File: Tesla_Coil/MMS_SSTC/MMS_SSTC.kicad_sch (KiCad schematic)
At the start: 57 parts, among them J1 Screw_Terminal_01x02, J2 Screw_Terminal_01x02, J3 Screw_Terminal_01x02, J4 Screw_Terminal_01x02, Q1 IRFP460APBF, U1 LM7812_TO220, U2 LM7805_TO220, U3 CD74HC14E, U4 UCC27524P, U5 NE555P

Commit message: Begin work on final tesla coil design
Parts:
- removed AE1: Antenna, TestPoint:TestPoint_Keystone_5000-5004_Miniature, symbol Device:Antenna
- removed C1, C3: 470u, Capacitor_THT:CP_Radial_D12.5mm_P5.00mm, symbol Device:C_Polarized_Small
- removed C13, C17: 10n, Capacitor_THT:C_Disc_D5.0mm_W2.5mm_P2.50mm, symbol Device:C_Small
- removed C15, C16: 1.5n, Capacitor_THT:C_Rect_L13.0mm_W4.0mm_P10.00mm_FKS3_FKP3_MKS4, symbol Device:C_Small
- removed C2, C4, C5: 0.1u, Capacitor_THT:C_Disc_D3.0mm_W2.0mm_P2.50mm, symbol Device:C_Small
- removed C6, C7: 2200u, Capacitor_THT:CP_Radial_D25.0mm_P10.00mm_SnapIn, symbol Device:C_Polarized_Small
- removed C8: 0.68u, Capacitor_THT:C_Rect_L7.2mm_W5.5mm_P5.00mm_FKS2_FKP2_MKS2_MKP2, symbol Device:C_Small
- removed D1: D_Filled, Diode_THT:D_DO-41_SOD81_P7.62mm_Horizontal, symbol Device:D_Filled
- removed D2: B125C2300-1500A, Diode_THT:Diode_Bridge_Vishay_GBU, symbol Diode_Bridge:B125C2300-1500A
- removed D3, D6: ~, Diode_THT:D_DO-41_SOD81_P7.62mm_Horizontal, symbol Device:D_Small_Filled
- removed J1, J3: Screw_Terminal_01x02, locals:691137710003, symbol Connector:Screw_Terminal_01x03
- removed J2: Screw_Terminal_01x02, locals:691137710002, symbol Connector:Screw_Terminal_01x02
- removed JP1, JP3, JP4: Jumper_2_Bridged, TestPoint:TestPoint_Bridge_Pitch2.54mm_Drill0.7mm, symbol Jumper:Jumper_2_Bridged
- removed JP2, JP5: Jumper_2_Open, TestPoint:TestPoint_Bridge_Pitch2.54mm_Drill0.7mm, symbol Jumper:Jumper_2_Open
- removed R2: 220k, Resistor_THT:R_Axial_DIN0204_L3.6mm_D1.6mm_P5.08mm_Horizontal, symbol Device:R_US
- removed R5: 1k, Resistor_THT:R_Axial_DIN0204_L3.6mm_D1.6mm_P5.08mm_Horizontal, symbol Device:R_US
- removed TR1: 48VAC, symbol Transformer:TRANSF4
- removed U1: LM7812_TO220, Package_TO_SOT_THT:TO-220-3_Vertical, symbol Regulator_Linear:LM7812_TO220
- removed U2: LM7805_TO220, Package_TO_SOT_THT:TO-220-3_Vertical, symbol Regulator_Linear:LM7805_TO220
- removed U4: UCC27524P, Package_DIP:DIP-8_W7.62mm, symbol locals:UCC27524P
- added D3: 400V, Diode_THT:D_DO-27_P12.70mm_Horizontal, symbol Device:D_TVS_Small_Filled
- added U6: UCC37322P, UCC37322P:DIP794W45P254L959H508Q8, symbol locals:UCC37322P
- C14: value 1.5n -> 2.7n; DKPN 495-3205-ND -> 495-3223-ND
- Q1: value IRFP460APBF -> FQA8N100C; DKPN IRFP460APBF-ND -> FQA8N100CFS-ND
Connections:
- net +12V: now also U6.1 (VDD__1), U6.8 (VDD)
- net Earth: no longer C10.1, C11.1, C12.2, C14.2, C18.2, C19.2, C9.2, D4.1 (A1), D5.1 (A1), Q1.3 (S), U3.7 (GND), U5.1 (GND), U5.7 (DIS)
- net INTERRUPT_OUT: now also U6.3 (ENBL)
- net OSC_OUT: now also U6.2 (IN)
- net at R1.2: now also U6.6 (OUT), U6.7 (OUT__1)
- net at C14.1, J4.3 (Pin_3), Q1.2 (D): now also D3.2 (A2); no longer D4.2 (A2)
- net +68V renamed +170V
- new net: D3.1 (A1), D4.2 (A2)
- new net GND: C10.1, C11.1, C12.2, C14.2, C18.2, C19.2, C9.2, D4.1 (A1), D5.1 (A1), Q1.3 (S), U3.7 (GND), U5.1 (GND), U5.7 (DIS), U6.4 (AGND), U6.5 (PGND)
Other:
- note added: "2x 1.5n 5% also viable but less tolerance stackup will make things easier"
- note added: "EARTH GROUND ONLY!"
- note added: "Note: C19 should be stable and well toleranced if using fixed values"
- note added: "renumber this bs for the schematic later"
- note added: "terminal blocks for primary coil need to be impossible to touch when put together"
- note removed: "150k also viable"
- note removed: "Antenna feedback: Connect JP3, disconnect JP4 Oscillator: Disonnect JP3, connect JP4 C/W output: Disconnect JP2, connect JP1 Antenna cap test: Disconnect JP5"
- note removed: "D3 and D6 *must* have forward voltage <0.5 and be schottky"
- note removed: "Note: C19 should be stable and high quality if using fixed values"
- note removed: "Primary between 2-3 Secondary ground on 1"
- note removed: "R5 for current limiting short if problems"
- note removed: "Try desoldering one of the big caps just to see what happens"
- note removed: "power delivery deserves its own separate page </3"
- moved on the sheet: C10, C11, C12, C14, C18, C19, C9, D4, D5, D7, D8, J4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

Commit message: Draft BOM for final SSTC design
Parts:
- removed D8: D_Small_Filled, Diode_THT:D_DO-41_SOD81_P7.62mm_Horizontal, symbol Device:D_Small_Filled
- removed R3: 1k, Resistor_THT:R_Axial_DIN0204_L3.6mm_D1.6mm_P5.08mm_Horizontal, symbol Device:R_US
- removed RV2, RV3: R_Potentiometer_Trim_US, Potentiometer_THT:Potentiometer_Bourns_3296W_Vertical, symbol Device:R_Potentiometer_Trim_US
- added R1: 18k, Resistor_THT:R_Axial_DIN0204_L3.6mm_D1.6mm_P5.08mm_Horizontal, symbol Device:R_Small_US
- added R2: 150k, Resistor_THT:R_Axial_DIN0204_L3.6mm_D1.6mm_P5.08mm_Horizontal, symbol Device:R_Small_US
- D1: renamed from D7; footprint Diode_THT:D_DO-41_SOD81_P7.62mm_Horizontal -> Diode_THT:D_DO-35_SOD27_P7.62mm_Horizontal; DKPN 1N4004-TPMSCT-ND -> 497-2499-1-ND
- RV1: footprint Potentiometer_THT:Potentiometer_Bourns_3296W_Vertical -> Potentiometer_THT:Potentiometer_Bourns_3296X_Horizontal; DKPN 118-3296W-1-103RLFCT-ND -> 118-3296X-1-222LF-ND
- U1: renamed from U5; footprint Package_DIP:DIP-8_W7.62mm -> Package_DIP:DIP-8_W7.62mm_Socket
- U2: renamed from U6; footprint UCC37322P:DIP794W45P254L959H508Q8 -> Package_DIP:DIP-8_W7.62mm_Socket
- renumbered AE2 to AE1, C18 to C1, C12 to C2, C19 to C3, C9 to C4, C11 to C5, C14 to C6, C10 to C7, D5 to D2, J4 to J1, R1 to R3
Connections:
- net GND: no longer U1.7 (DIS)
- net INTERRUPT_OUT: now also D1.2 (A)
- net at C3.1, U1.2 (TR), U1.6 (THR): now also R1.2, R2.2
- net at D1.1 (K): now also R1.1
- new net: R2.1, U1.7 (DIS)
- no-connect marks 11 -> 9
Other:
- moved on the sheet: C2, C3, D1

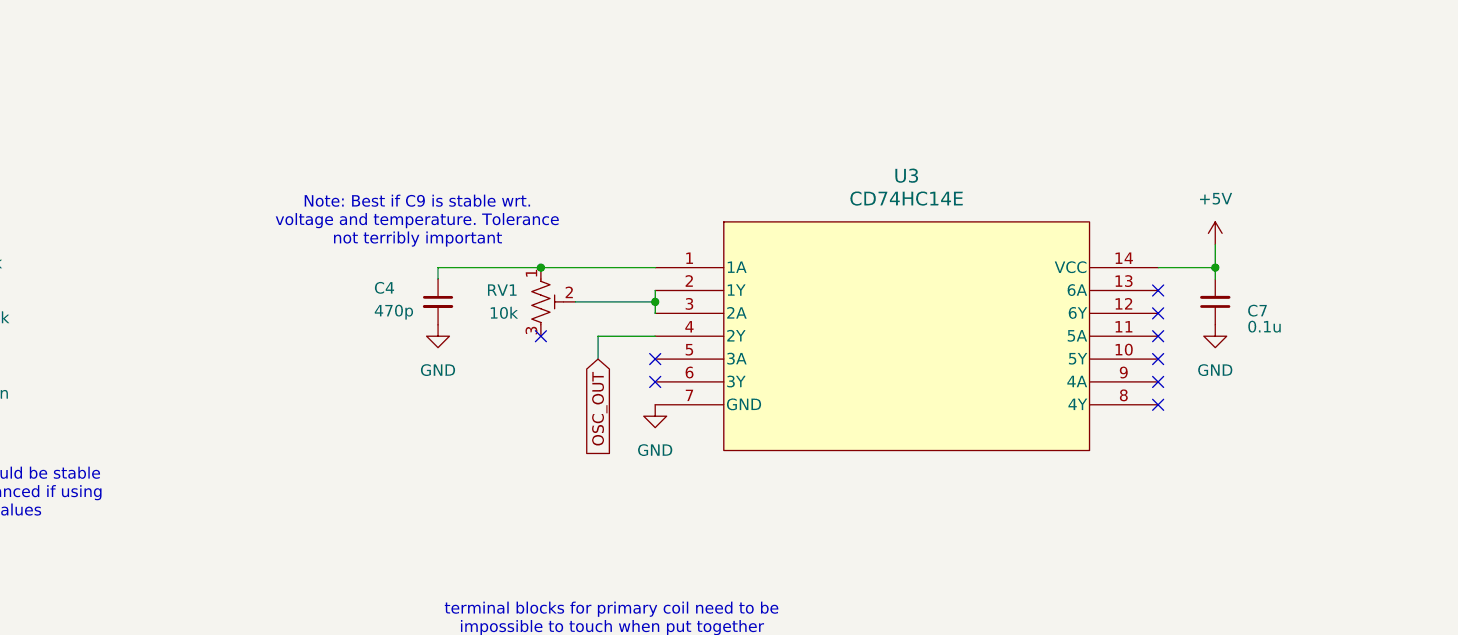
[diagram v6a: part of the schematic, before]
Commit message: apply cost saving measures
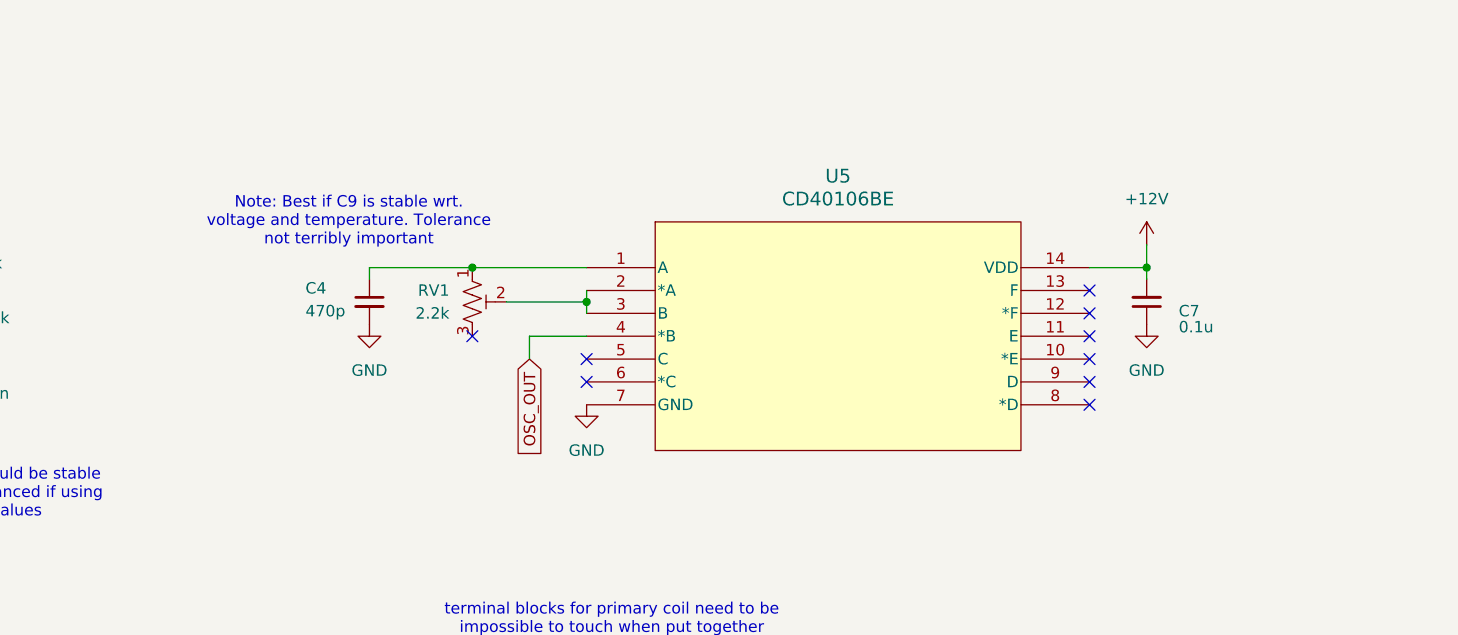
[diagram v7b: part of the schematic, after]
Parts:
- removed U3: CD74HC14E, Package_DIP:DIP-14_W7.62mm, symbol locals:CD74HC14E
- added U5: CD40106BE, N14, symbol locals:CD40106BE
- AE1: now left out of the parts list
- RV1: value 10k -> 2.2k
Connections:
- net +5V is gone; now on net +12V: C7.2
- net +12V: now also U5.14 (VDD)
- net GND: now also U5.7 (GND)
- net OSC_OUT: now also U5.4 (*B)
- net at C4.1, RV1.1: now also U5.1 (A)
- net at RV1.2: now also U5.2 (*A), U5.3 (B)
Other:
- moved on the sheet: C4, C7, RV1

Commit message: Rough layout on final SSTC PCB
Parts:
- removed U5: CD40106BE, N14, symbol locals:CD40106BE
- added JP1: SolderJumper_2_Open, Jumper:SolderJumper-2_P1.3mm_Open_RoundedPad1.0x1.5mm, symbol Jumper:SolderJumper_2_Open
- added R6: 1.8k, Resistor_THT:R_Axial_DIN0204_L3.6mm_D1.6mm_P5.08mm_Horizontal, symbol Device:R_Small_US
- added R7: 1.5k, Resistor_THT:R_Axial_DIN0204_L3.6mm_D1.6mm_P5.08mm_Horizontal, symbol Device:R_Small_US
- added U3: CD74HC14E, N14, symbol locals:CD74HC14E
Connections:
- net +12V: now also JP1.2 (B), R6.1; no longer C7.2
- net GND: now also R7.2, U3.7 (GND)
- net OSC_OUT: now also U3.4 (2Y)
- net at C4.1, RV1.1: now also U3.1 (1A)
- net at RV1.2: now also U3.2 (1Y), U3.3 (2A)
- new net: C7.2, JP1.1 (A), R6.2, R7.1, U3.14 (VCC)
